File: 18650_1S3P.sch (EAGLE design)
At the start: 27 parts, among them Q1 DMG3404, Q2 DMG3404, Q3 DMG3404, Q4 DMG3404

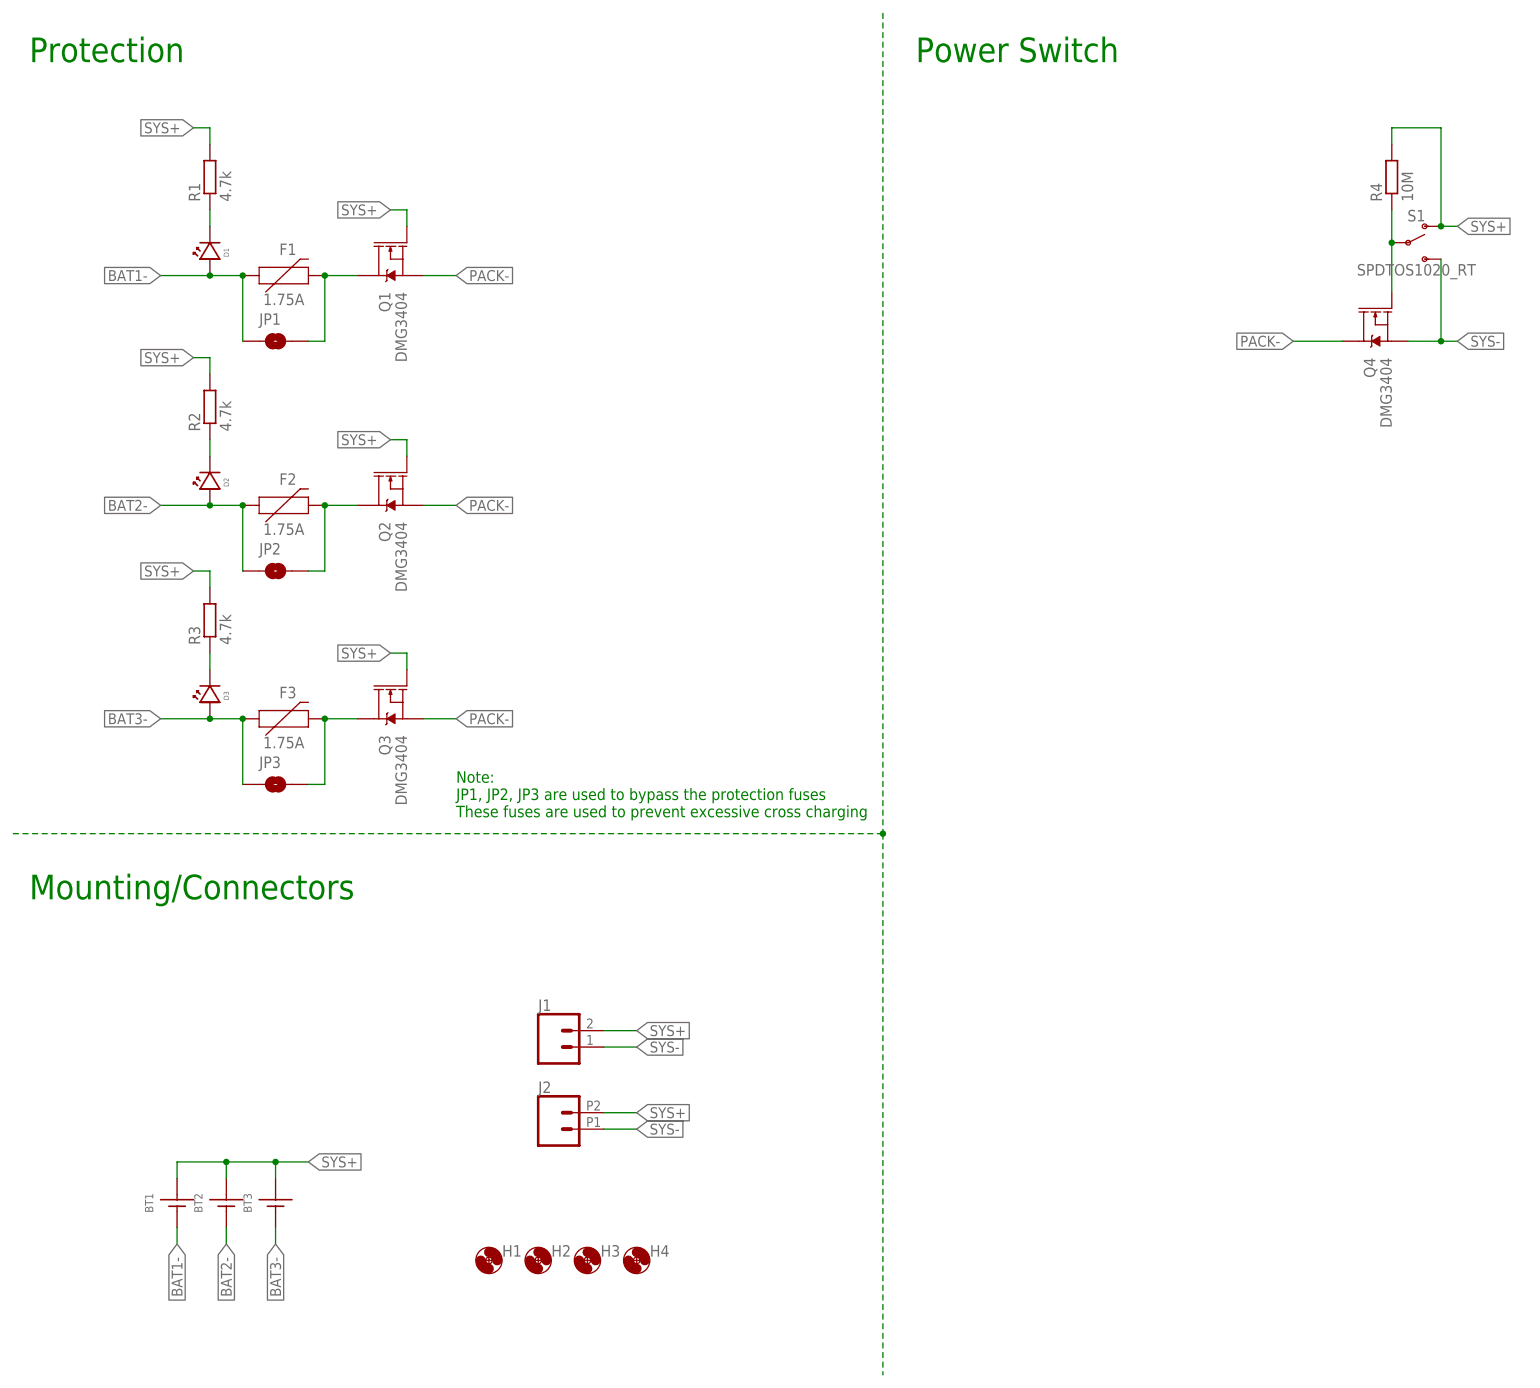
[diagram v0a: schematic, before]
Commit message: Update for v0.1 system
Updated system to v0.1, changed switching and reverse polarity protection system, ready for fab
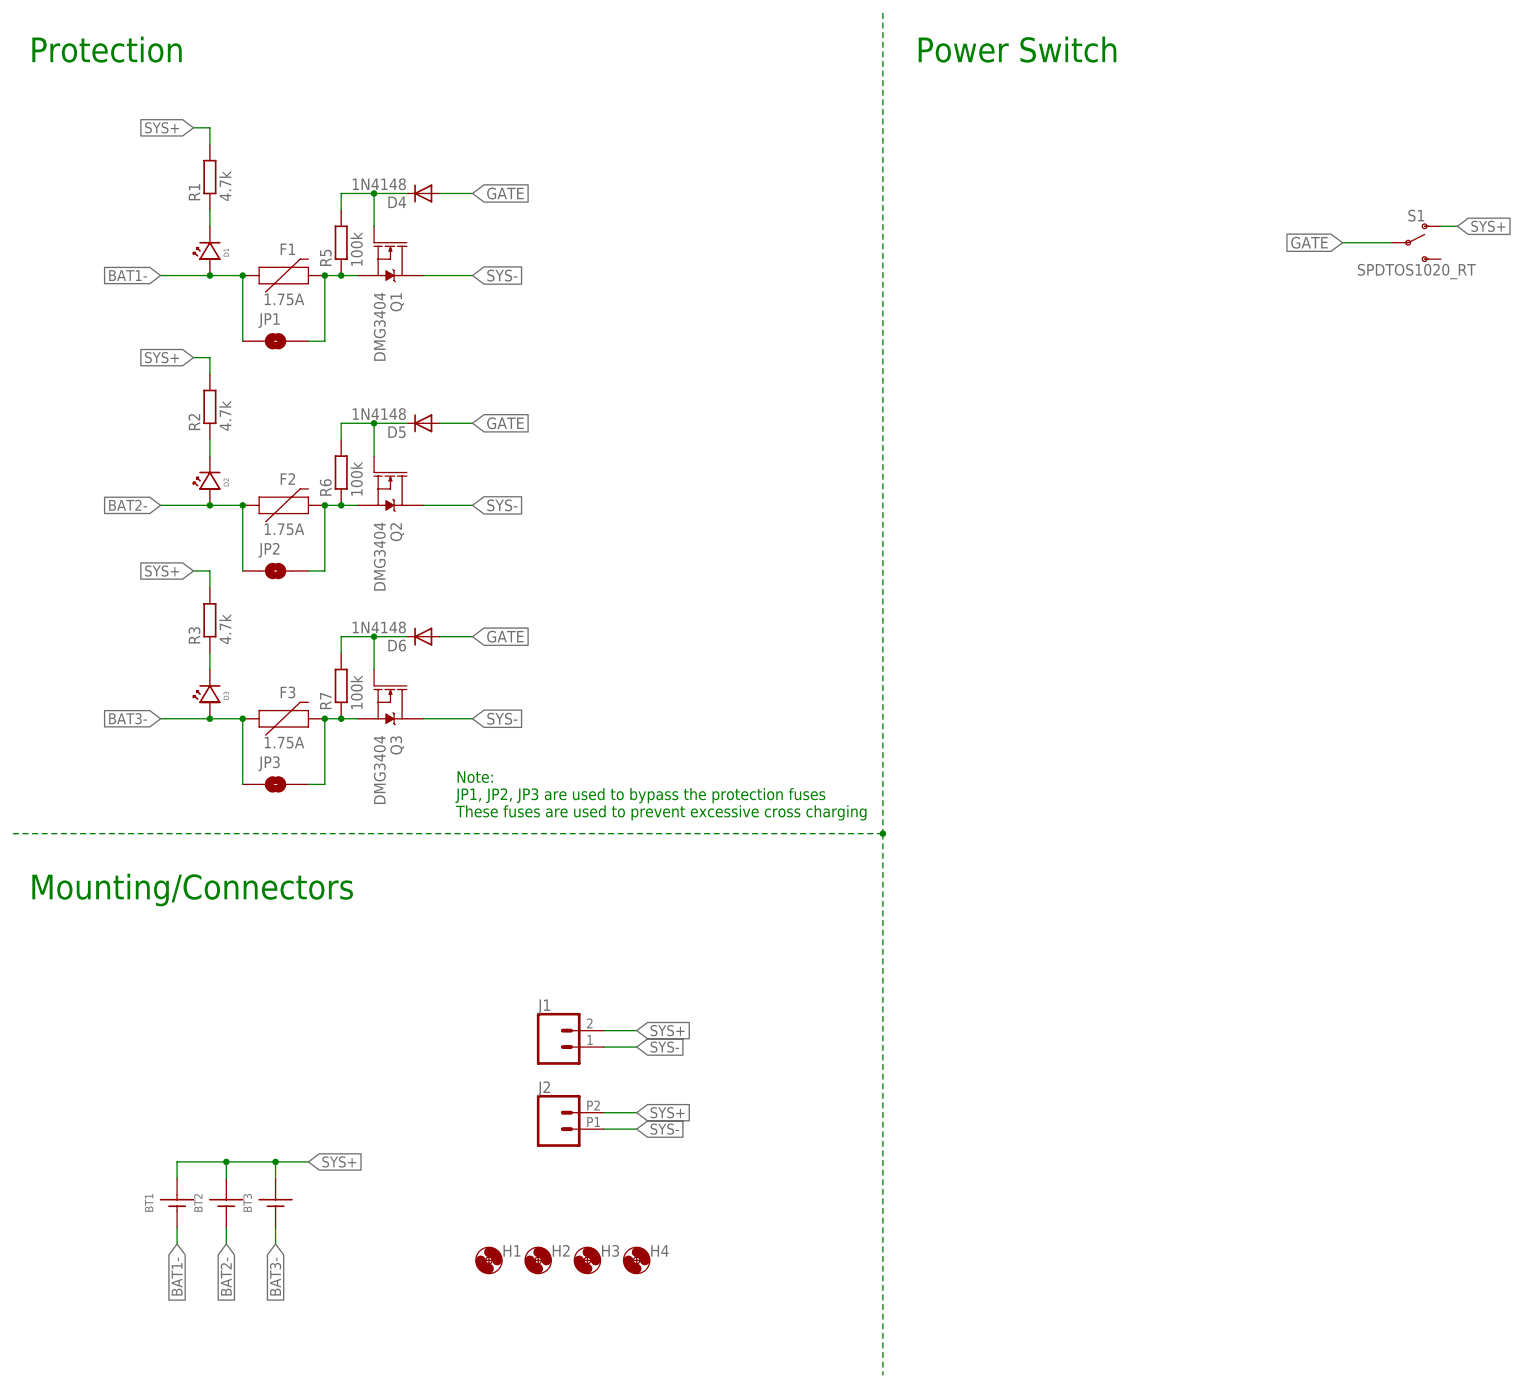
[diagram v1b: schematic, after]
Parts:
- removed Q4: DMG3404, bschulz:MOSFET-NCH-DMG3404L
- removed R4: 10M, bschulz_passives:R-EU_10MR0603
- added D4, D5, D6: 1N4148, bschulz:DIODESOD-323
- added R5, R6, R7: 100k, bschulz_passives:R-EU_100KR0603
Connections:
- removed net N$7: Q4.G, R4.1, S1.P
- removed net PACK-: Q1.S, Q2.S, Q3.S, Q4.D
- new net GATE: D4.A, D5.A, D6.A, S1.P
- new net N$10: D4.C, Q1.G, R5.2
- new net N$11: D6.C, Q3.G, R7.2
- new net N$9: D5.C, Q2.G, R6.2
- net N$3: now also Q1.S, R5.1; no longer Q1.D
- net N$4: now also Q2.S, R6.1; no longer Q2.D
- net N$6: now also Q3.S, R7.1; no longer Q3.D
- net SYS+: no longer Q1.G, Q2.G, Q3.G, R4.2
- net SYS-: now also Q1.D, Q2.D, Q3.D; no longer Q4.S, S1.S
